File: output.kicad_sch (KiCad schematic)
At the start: 70 parts, among them Q1 BC817, Q10 BC817, Q11 BC817, Q12 BC817, Q13 BC817, Q14 BC817, Q2 BC817, Q3 BC817, Q4 BC817, Q5 BC817, Q6 BC817, Q7 BC817, Q8 BC817, Q9 BC817, U20 PC817, U21 PC817, U22 PC817, U23 PC817, U24 PC817, U25 PC817, U26 PC817, U27 PC817, U28 PC817, U29 PC817, U30 PC817, U31 PC817, U32 PC817, U33 PC817

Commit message: trace pcb
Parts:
- removed D13, D14: 1N4007, Diode_SMD:D_SMA_Handsoldering, symbol Diode:1N4007
- removed Q13, Q14: BC817, Package_TO_SOT_SMD:SOT-23, symbol Transistor_BJT:BC817
- removed R41, R42, R43, R44: 680, Resistor_SMD:R_0805_2012Metric_Pad1.20x1.40mm_HandSolder, symbol Device:R
- removed U32, U33: PC817, Package_DIP:DIP-4_W7.62mm, symbol Isolator:PC817
- renumbered R17 to R18, R18 to R19, R19 to R20, R20 to R21, R21 to R22, R22 to R23, R23 to R24, R24 to R25, R25 to R26, R26 to R27, R27 to R28, R28 to R29, R29 to R30, R30 to R31, R31 to R32, R32 to R33, R33 to R34, R34 to R35, R35 to R36, R36 to R37, R37 to R38, R38 to R39, R39 to R40, R40 to R41, U20 to U19, U21 to U20, U22 to U21, U23 to U22, U24 to U23, U25 to U24, U26 to U25, U27 to U26, U28 to U27, U29 to U28, U30 to U29, U31 to U30
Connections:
- net GND: no longer Q1.2 (E), Q10.2 (E), Q11.2 (E), Q12.2 (E), Q2.2 (E), Q3.2 (E), Q4.2 (E), Q5.2 (E), Q6.2 (E), Q7.2 (E), Q8.2 (E), Q9.2 (E)
- new net GND_IN: Q1.2 (E), Q10.2 (E), Q11.2 (E), Q12.2 (E), Q2.2 (E), Q3.2 (E), Q4.2 (E), Q5.2 (E), Q6.2 (E), Q7.2 (E), Q8.2 (E), Q9.2 (E)

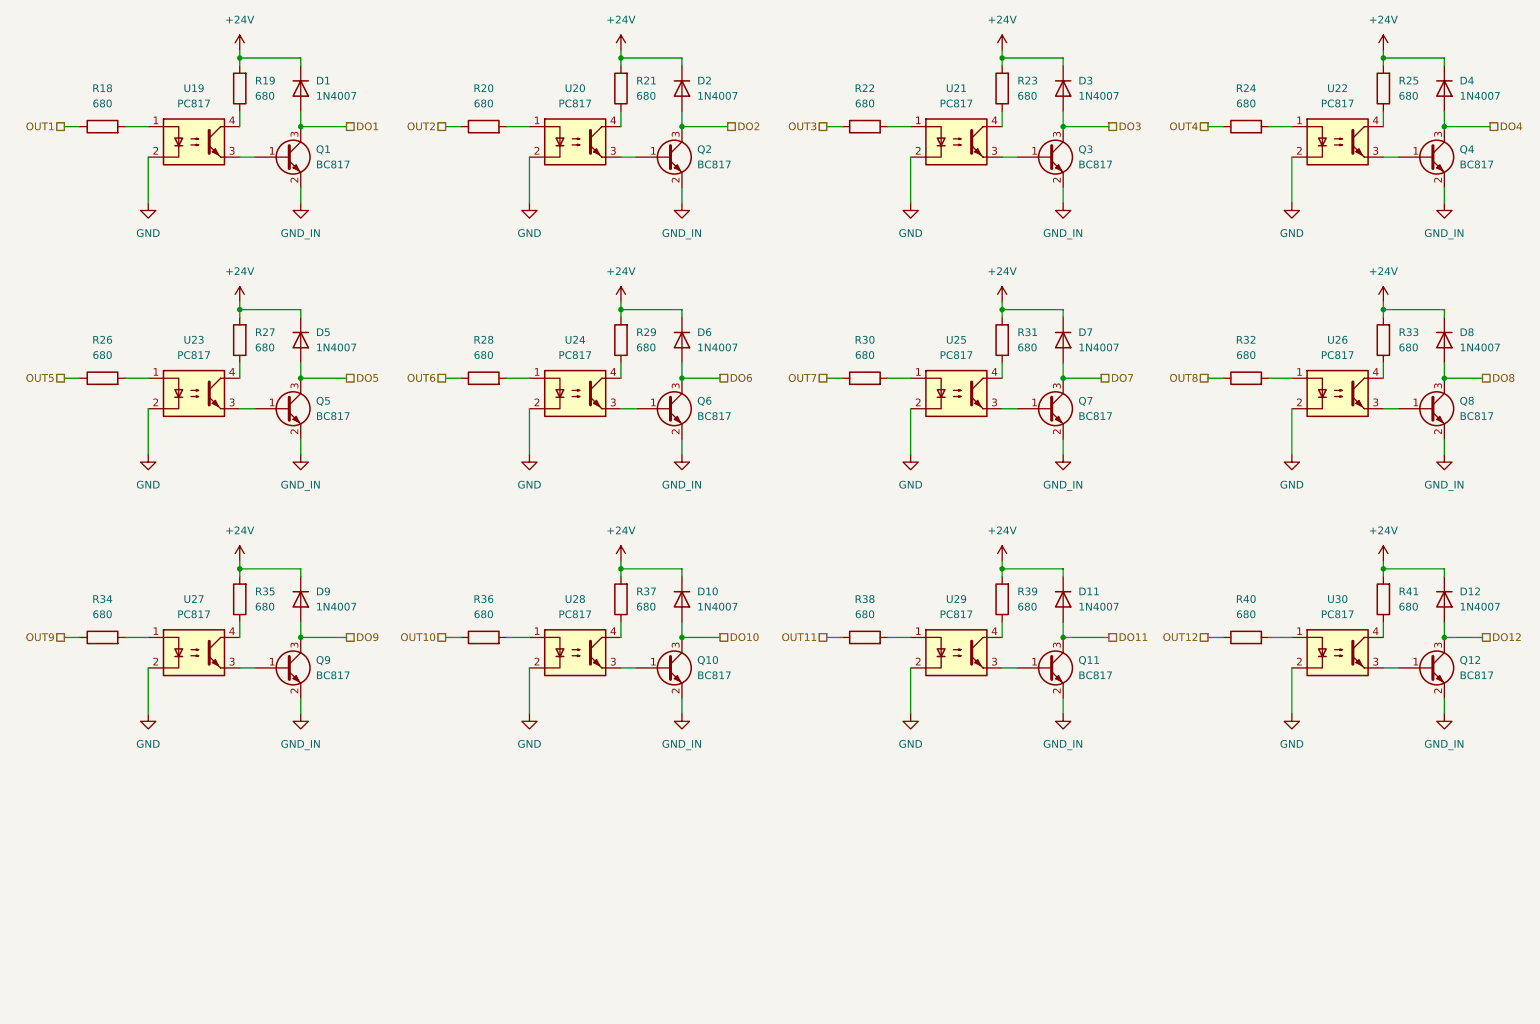
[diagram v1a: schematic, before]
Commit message: update to kicad 9
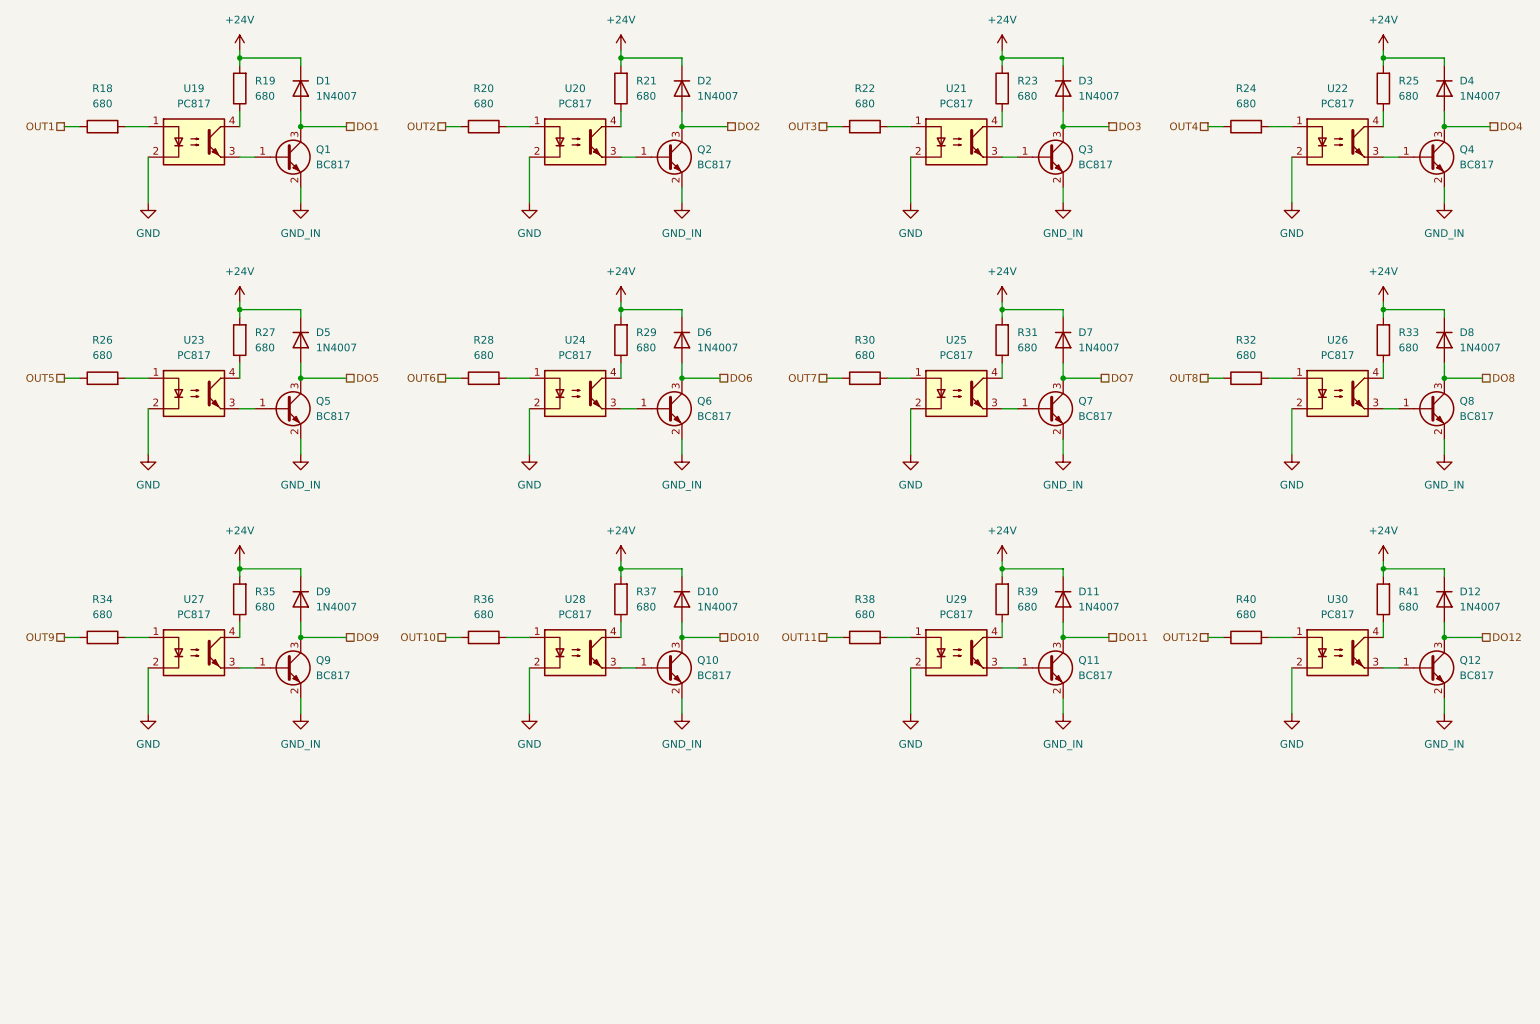
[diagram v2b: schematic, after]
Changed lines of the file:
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@@
 (kicad_sch
-	(version 20231120)
+	(version 20250114)
 	(generator "eeschema")
-	(generator_version "8.0")
+	(generator_version "9.0")
 	(paper "A4")
 	(junction
